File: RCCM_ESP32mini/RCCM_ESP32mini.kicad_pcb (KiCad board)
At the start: 2 copper layers, 38.1 x 49.5 mm, 16 parts, among them CN1 Conn_02x04_Odd_Even, CN2 Conn_01x08, CN3 Conn_01x07, CN4 Conn_01x06, CN5 Conn_01x06, CN6 Conn_02x10_Odd_Even, CN7 Conn_02x10_Odd_Even, CN8 Conn_01x06, J1 Conn_01x02, U1 LT1129-3.3_SOT223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

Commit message: Gerber change
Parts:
- added J2: Conn_01x02, Pin_Headers:Pin_Header_Straight_2x01_Pitch2.54mm, F.Cu at (86.4, 76.2)
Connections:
- CN5 pad 2: (no net) -> MODEd
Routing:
- net Vin: track 66.1 -> 93.5 mm
- net 3V3e: track 85.9 -> 100.9 mm
- net GND: track 114.4 -> 128.8 mm
- net Aout1: track 8.49 -> 19.2 mm
- net Aout2: track 7.47 -> 14.9 mm
- net MODEd: track 0.00 -> 7.40 mm
- net IO18: track 31.6 -> 39.0 mm
- net Bout2: track 7.27 -> 14.5 mm
- net VCCe: track 41.4 -> 48.6 mm
- net Bout1: track 6.45 -> 13.2 mm
- net IO19: track 39.2 -> 32.8 mm
- net IO32: track 12.3 -> 17.8 mm
- net AIN2: track 39.7 -> 43.4 mm, vias 0 -> 1
- net IO05: track 21.0 -> 23.6 mm
- net AIN1: track 53.6 -> 51.7 mm
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- added copper zone on B.Cu, net GND
- added copper zone on F.Cu, net GND
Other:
- net class MTR: trace_width 0.5 -> 1.7

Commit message: Gerber Update
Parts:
- added G***: LOGO, logos:RumiCar1_3p3, B.Cu at (101.6, 50.8)
- added G***: LOGO, logos:RumiCar3_3p3, B.Cu at (94.0, 50.8)
- added G***: LOGO, logos:ALGYAN2p5, B.Cu at (95.9, 54.0)
- CN1: moved to B.Cu
- moved CN1 7.62 mm to (99.1, 47.0)
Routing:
- net GND: track 128.8 -> 194.6 mm, vias 0 -> 12
- net IO21: track 19.8 -> 37.0 mm
- net Vin: track 93.5 -> 84.2 mm
- net 3V3e: track 100.9 -> 109.0 mm
- net IO22: track 21.1 -> 27.0 mm
- net IO05: track 23.6 -> 27.7 mm
- net IO32: track 17.8 -> 21.2 mm
- net IO18: track 39.0 -> 41.1 mm
- net BIN2: track 56.6 -> 58.7 mm
- net BIN1: track 62.5 -> 63.7 mm
- net AIN2: track 43.4 -> 44.2 mm
- net IO19: track 32.8 -> 32.2 mm
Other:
- outline, holes or cut-outs redrawn
- board text added: "A.W. S.Inatama"
- board text added: "G"
- board text added: "G B2 B1 A2 A1 V"
- board text added: "RumiCar CM ESP32mini"
- board text added: "VCC"
- board text added: "VM"
- board text added: "Vi/Vo/G/- Vi/G/Vo"

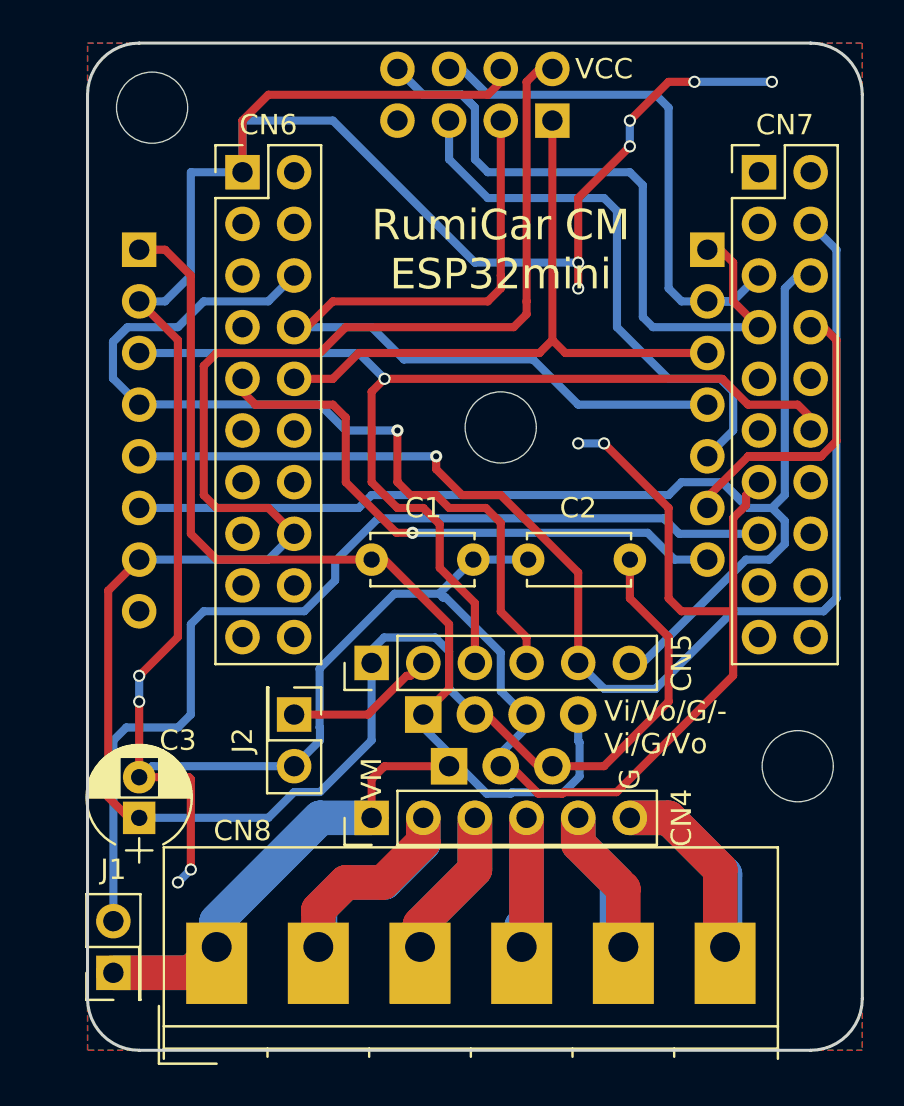
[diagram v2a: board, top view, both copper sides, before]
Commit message: SDx Update
(No:Pos:SDx:CNx:Nano:ESP32:M5S),
(S1:LEFT:SD0:CN1-5:No14:IO19:NC),
(S2:CEN:SD1:CN1-3:No15:IO18:G32),
(S3:RIGHT:SD2:CN1-1:No16:IO5:G33)
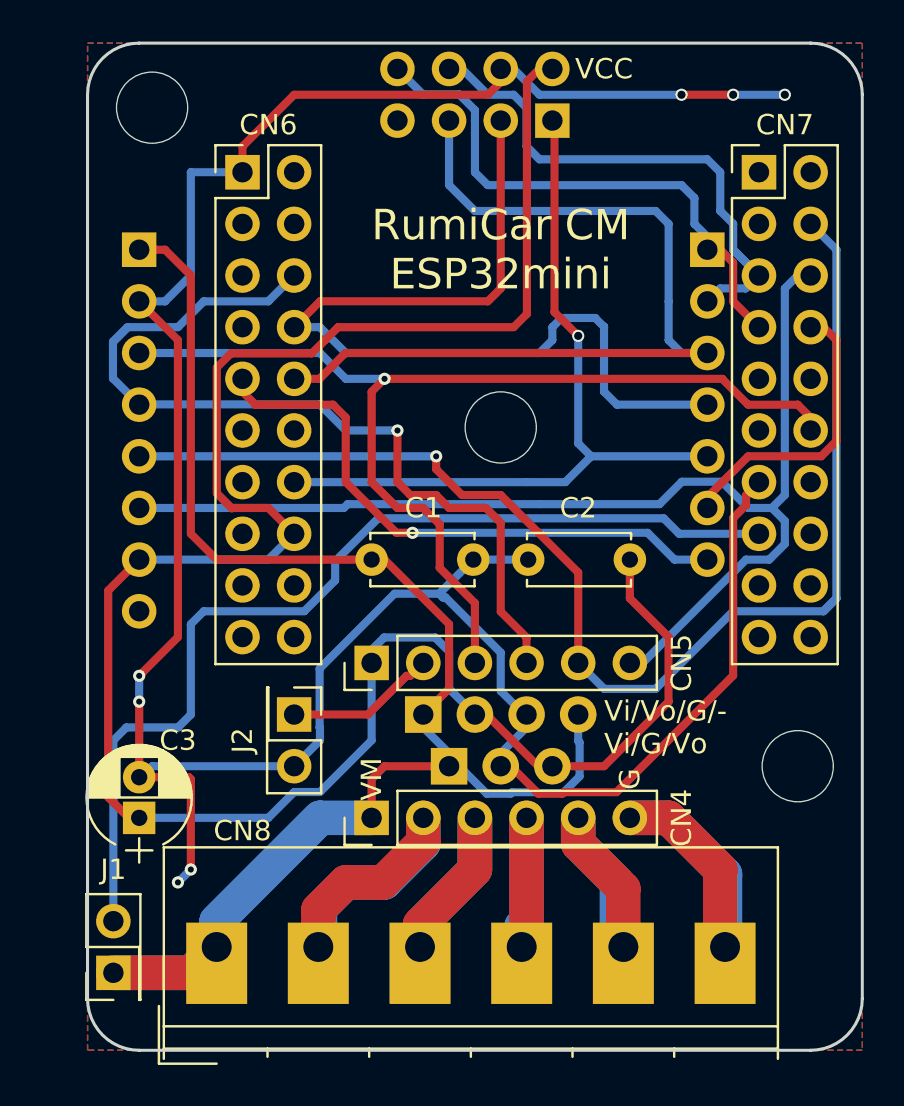
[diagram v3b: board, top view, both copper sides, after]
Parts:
- renumbered G*** to L1, G*** to L2, G*** to L3
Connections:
- CN1 pad 1: IO19 -> IO05
- CN1 pad 5: IO05 -> IO19
- CN6 pad 14: (no net) -> IO05
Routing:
- net GND: track 194.6 -> 156.3 mm, vias 12 -> 7
- net IO19: track 32.2 -> 43.5 mm
- net IO05: track 27.7 -> 38.1 mm, vias 0 -> 1
- net IO21: track 37.0 -> 27.7 mm
- net IO32: track 21.2 -> 14.5 mm
- net IO18: track 41.1 -> 45.4 mm
- net BIN2: track 58.7 -> 56.9 mm
- net 3V3e: track 109.0 -> 107.7 mm

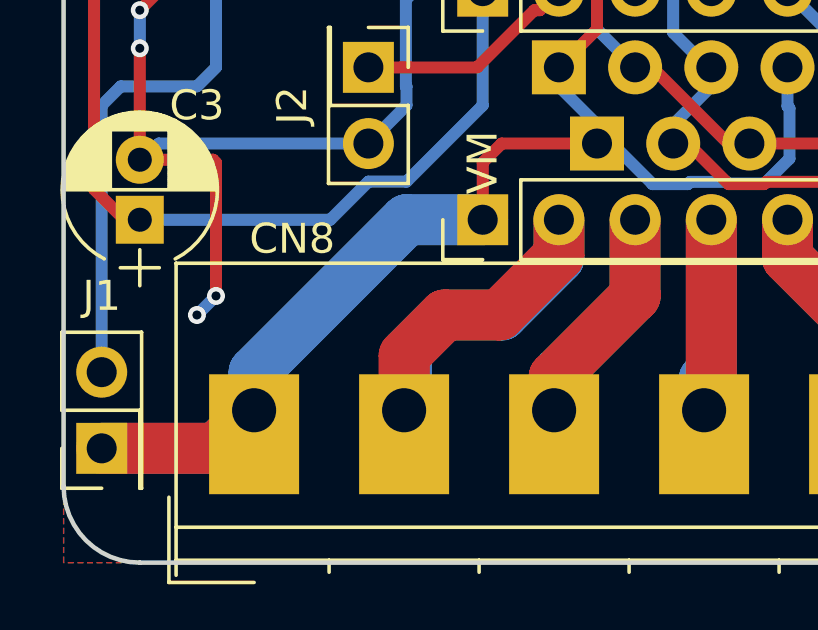
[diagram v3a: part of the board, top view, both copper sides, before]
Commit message: Add Panelized Gerber
xxx-Gerber-P is Panelized data.
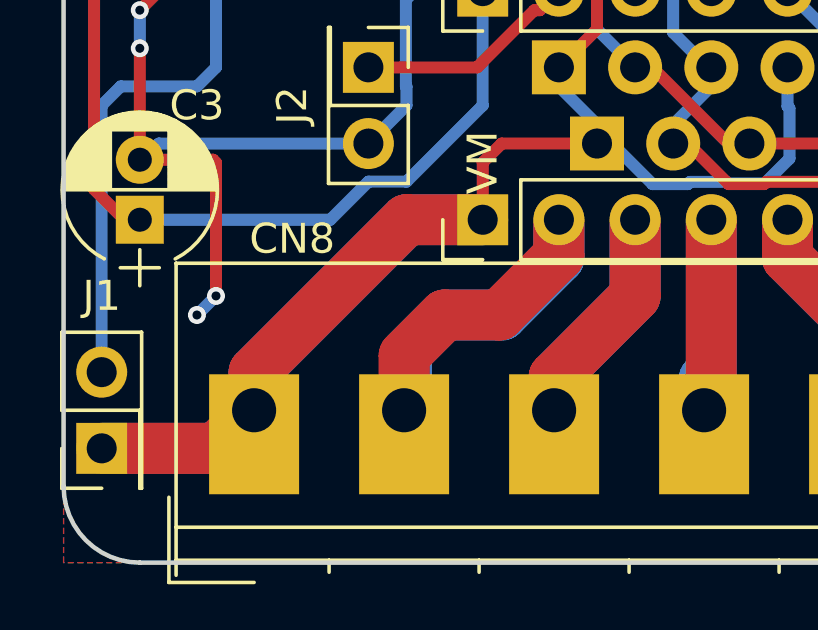
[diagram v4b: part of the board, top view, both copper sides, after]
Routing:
- net Vin: track 84.2 -> 95.1 mm
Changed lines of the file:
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@@
     (thickness 1.6)
     (drawings 26)
-    (tracks 369)
+    (tracks 372)
     (zones 0)
     (modules 20)
@@
       (drillshape 0)
       (scaleselection 1)
-      (outputdirectory Gerber/))
+      (outputdirectory ESP-Gerber/))
   )
   (net 0 "")
@@
     (add_net Bout1)
     (add_net Bout2)
+    (add_net Vin)
   )
   (net_class SIG ""
@@
     (add_net MODEd)
     (add_net VCCe)
-    (add_net Vin)
   )
   (module Capacitors_THT:C_Disc_D5.0mm_W2.5mm_P5.00mm (layer F.Cu)
@@
     (arrow2b (pts (xy 60.96 81.28) (xy 60.373579 80.153496)))
   )
+  (segment (start 90.17 81.28) (end 87.63 81.28) (width 1.7) (layer F.Cu) (net 1))
+  (segment (start 87.63 81.28) (end 82.55 86.36) (width 1.7) (layer F.Cu) (net 1))
+  (segment (start 82.55 86.36) (end 82.55 87.63) (width 1.7) (layer F.Cu) (net 1))
   (segment (start 90.17 79.375) (end 90.17 81.28) (width 0.4) (layer F.Cu) (net 1))
   (segment (start 90.805 78.74) (end 90.17 79.375) (width 0.4) (layer F.Cu) (net 1))
@@
   (segment (start 107.315 51.435) (end 107.95 52.07) (width 0.4) (layer B.Cu) (net 7))
   (segment (start 107.95 52.07) (end 107.95 53.34) (width 0.4) (layer B.Cu) (net 7))
-  (segment (start 107.95 53.34) (end 109.22 54.61) (width 0.4) (layer B.Cu) (net 7) (status 800000))
+  (segment (start 107.95 53.34) (end 109.22 54.61) (width 0.4) (layer B.Cu) (net 7))
   (segment (start 97.79 48.26) (end 98.425 48.895) (width 0.4) (layer B.Cu) (net 7))
   (segment (start 107.315 49.53) (end 107.315 51.435) (width 0.4) (layer B.Cu) (net 7))
